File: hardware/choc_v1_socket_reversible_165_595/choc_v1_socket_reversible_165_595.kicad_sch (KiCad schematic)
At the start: 84 parts, among them SW00 SW_Push, SW01 SW_Push, SW02 SW_Push, SW03 SW_Push, SW04 SW_Push, SW05 SW_Push, SW10 SW_Push, SW11 SW_Push, SW12 SW_Push, SW13 SW_Push, SW14 SW_Push, SW15 SW_Push, SW20 SW_Push, SW21 SW_Push, SW22 SW_Push, SW23 SW_Push, SW24 SW_Push, SW25 SW_Push, SW26 SW_Push, SW30 SW_Push, SW31 SW_Push, SW32 SW_Push, SW33 SW_Push, SW34 SW_Push, SW35 SW_Push, SW36 SW_Push, U1 CH582

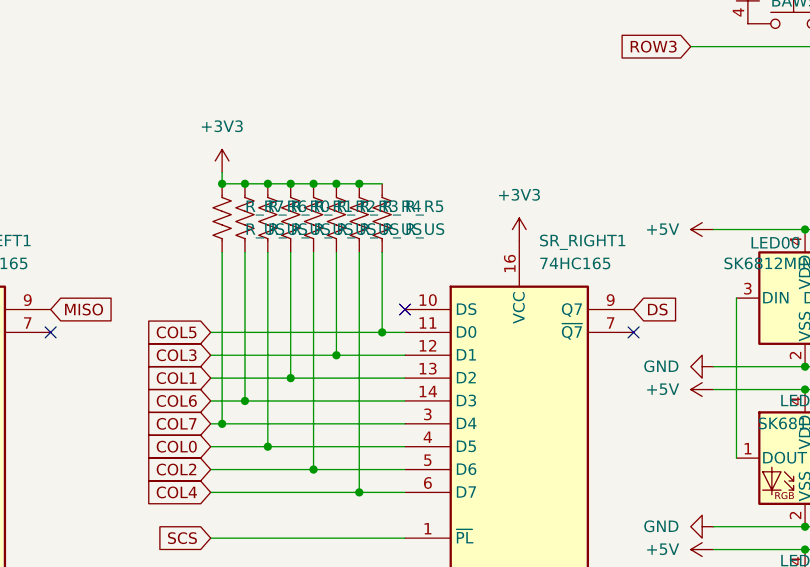
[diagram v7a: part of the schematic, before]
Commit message: Fixed Q7-SER connection
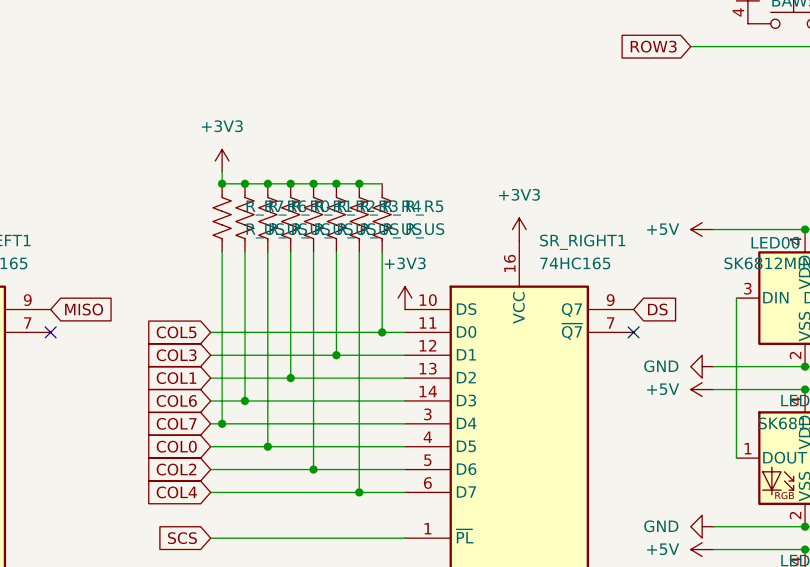
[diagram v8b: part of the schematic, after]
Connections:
- net +3V3: now also SR_RIGHT1.10 (DS)
- no-connect marks 17 -> 16
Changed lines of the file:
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@@
 	)
 	(no_connect
-		(at 107.95 102.87)
-	)
-	(no_connect
 		(at 72.39 45.72)
 	)
@@
 					(unit 1)
 				)
+			)
+		)
+	)
+	(symbol
+		(lib_id "power:+3V3")
+		(at 107.95 102.87 0)
+		(unit 1)
+		(exclude_from_sim no)
+		(in_bom yes)
+		(on_board yes)
+		(dnp no)
+		(fields_autoplaced yes)
+		(property "Reference" "#PWR22"
+			(at 107.95 106.68 0)
+			(effects
+				(font
+					(size 1.27 1.27)
+				)
+				(hide yes)
+			)
+		)
+		(property "Value" "+3V3"
+			(at 107.95 97.79 0)
+			(effects
+				(font
+					(size 1.27 1.27)
+				)
+			)
+		)
+		(property "Footprint" ""
+			(at 107.95 102.87 0)
+			(effects
+				(font
+					(size 1.27 1.27)
+				)
+				(hide yes)
+			)
+		)
+		(property "Datasheet" ""
+			(at 107.95 102.87 0)
+			(effects
+				(font
+					(size 1.27 1.27)
+				)
+				(hide yes)
+			)
+		)
+		(property "Description" "Power symbol creates a global label with name \"+3V3\""
+			(at 107.95 102.87 0)
+			(effects
+				(font
+					(size 1.27 1.27)
+				)
+				(hide yes)
+			)
+		)
+		(pin "1"
+		)
+		(instances
+			(project "choc_v1_socket_reversible_165_595"
+				(path "/1dbf748e-8163-44a2-a238-31b19fe70046"
+					(reference "#PWR22")
+					(unit 1)
+				)
